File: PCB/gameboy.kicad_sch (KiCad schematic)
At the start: 0 parts

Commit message: [+] pre-BOM push
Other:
- added sheet Audio (audio.kicad_sch)
- added sheet SD card (sd.kicad_sch)
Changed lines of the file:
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@@
+	)
+	(sheet
+		(at 118.745 77.47)
+		(size 25.4 18.415)
+		(fields_autoplaced yes)
+		(stroke
+			(width 0.1524)
+			(type solid)
+		)
+		(fill
+			(color 0 0 0 0.0000)
+		)
+		(property "Sheetname" "Audio"
+			(at 118.745 76.7584 0)
+			(effects
+				(font
+					(size 1.27 1.27)
+				)
+				(justify left bottom)
+			)
+		)
+		(property "Sheetfile" "audio.kicad_sch"
+			(at 118.745 96.4696 0)
+			(effects
+				(font
+					(size 1.27 1.27)
+				)
+				(justify left top)
+			)
+		)
+		(instances
+			(project "gameboy"
+				(path "/bfbf29d7-ad29-43e7-b23f-5805508cd3f0"
+					(page "5")
+				)
+			)
+		)
+	)
+	(sheet
+		(at 156.21 77.47)
+		(size 28.575 18.415)
+		(fields_autoplaced yes)
+		(stroke
+			(width 0.1524)
+			(type solid)
+		)
+		(fill
+			(color 0 0 0 0.0000)
+		)
+		(property "Sheetname" "SD card"
+			(at 156.21 76.7584 0)
+			(effects
+				(font
+					(size 1.27 1.27)
+				)
+				(justify left bottom)
+			)
+		)
+		(property "Sheetfile" "sd.kicad_sch"
+			(at 156.21 96.4696 0)
+			(effects
+				(font
+					(size 1.27 1.27)
+				)
+				(justify left top)
+			)
+		)
+		(instances
+			(project "gameboy"
+				(path "/bfbf29d7-ad29-43e7-b23f-5805508cd3f0"
+					(page "6")
+				)
+			)
+		)
 	)
 	(sheet

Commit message: some part done
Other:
- removed sheet Audio
- added sheet Peripherals (peripherals.kicad_sch)
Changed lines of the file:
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@@
-	)
-	(sheet
-		(at 118.745 77.47)
-		(size 25.4 18.415)
-		(fields_autoplaced yes)
-		(stroke
-			(width 0.1524)
-			(type solid)
-		)
-		(fill
-			(color 0 0 0 0.0000)
-		)
-		(property "Sheetname" "Audio"
-			(at 118.745 76.7584 0)
-			(effects
-				(font
-					(size 1.27 1.27)
-				)
-				(justify left bottom)
-			)
-		)
-		(property "Sheetfile" "audio.kicad_sch"
-			(at 118.745 96.4696 0)
-			(effects
-				(font
-					(size 1.27 1.27)
-				)
-				(justify left top)
-			)
-		)
-		(instances
-			(project "gameboy"
-				(path "/bfbf29d7-ad29-43e7-b23f-5805508cd3f0"
-					(page "5")
-				)
-			)
-		)
 	)
 	(sheet
@@
 				)
 			)
+		)
+	)
+	(sheet
+		(at 111.76 78.105)
+		(size 27.94 17.78)
+		(fields_autoplaced yes)
+		(stroke
+			(width 0.1524)
+			(type solid)
+		)
+		(fill
+			(color 0 0 0 0.0000)
+		)
+		(property "Sheetname" "Peripherals"
+			(at 111.76 77.3934 0)
+			(effects
+				(font
+					(size 1.27 1.27)
+				)
+				(justify left bottom)
+			)
+		)
+		(property "Sheetfile" "peripherals.kicad_sch"
+			(at 111.76 96.4696 0)
+			(effects
+				(font
+					(size 1.27 1.27)
+				)
+				(justify left top)
+			)
+		)
+		(instances
+			(project "gameboy"
+				(path "/bfbf29d7-ad29-43e7-b23f-5805508cd3f0"
+					(page "6")
+				)
+			)

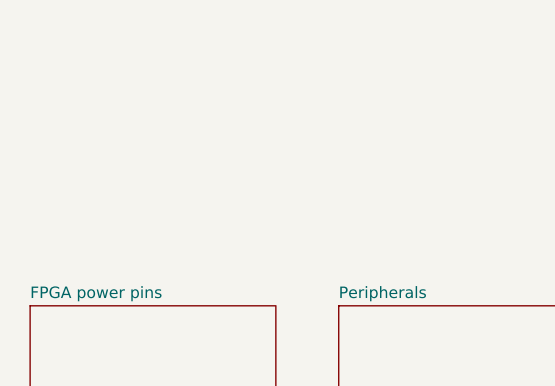
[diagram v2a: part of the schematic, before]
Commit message: [+] add ZynqPCB
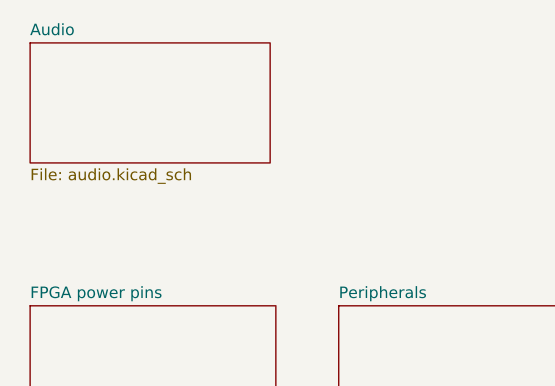
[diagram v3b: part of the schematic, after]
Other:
- added sheet Audio (audio.kicad_sch)
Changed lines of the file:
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@@
+	)
+	(sheet
+		(at 77.47 48.895)
+		(size 26.67 13.335)
+		(fields_autoplaced yes)
+		(stroke
+			(width 0.1524)
+			(type solid)
+		)
+		(fill
+			(color 0 0 0 0.0000)
+		)
+		(property "Sheetname" "Audio"
+			(at 77.47 48.1834 0)
+			(effects
+				(font
+					(size 1.27 1.27)
+				)
+				(justify left bottom)
+			)
+		)
+		(property "Sheetfile" "audio.kicad_sch"
+			(at 77.47 62.8146 0)
+			(effects
+				(font
+					(size 1.27 1.27)
+				)
+				(justify left top)
+			)
+		)
+		(property "Field2" ""
+			(at 77.47 48.895 0)
+			(effects
+				(font
+					(size 1.27 1.27)
+				)
+				(hide yes)
+			)
+		)
+		(instances
+			(project "gameboy"
+				(path "/bfbf29d7-ad29-43e7-b23f-5805508cd3f0"
+					(page "7")
+				)
+			)
+		)
 	)
 	(sheet
